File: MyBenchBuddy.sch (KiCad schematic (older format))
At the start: 0 parts

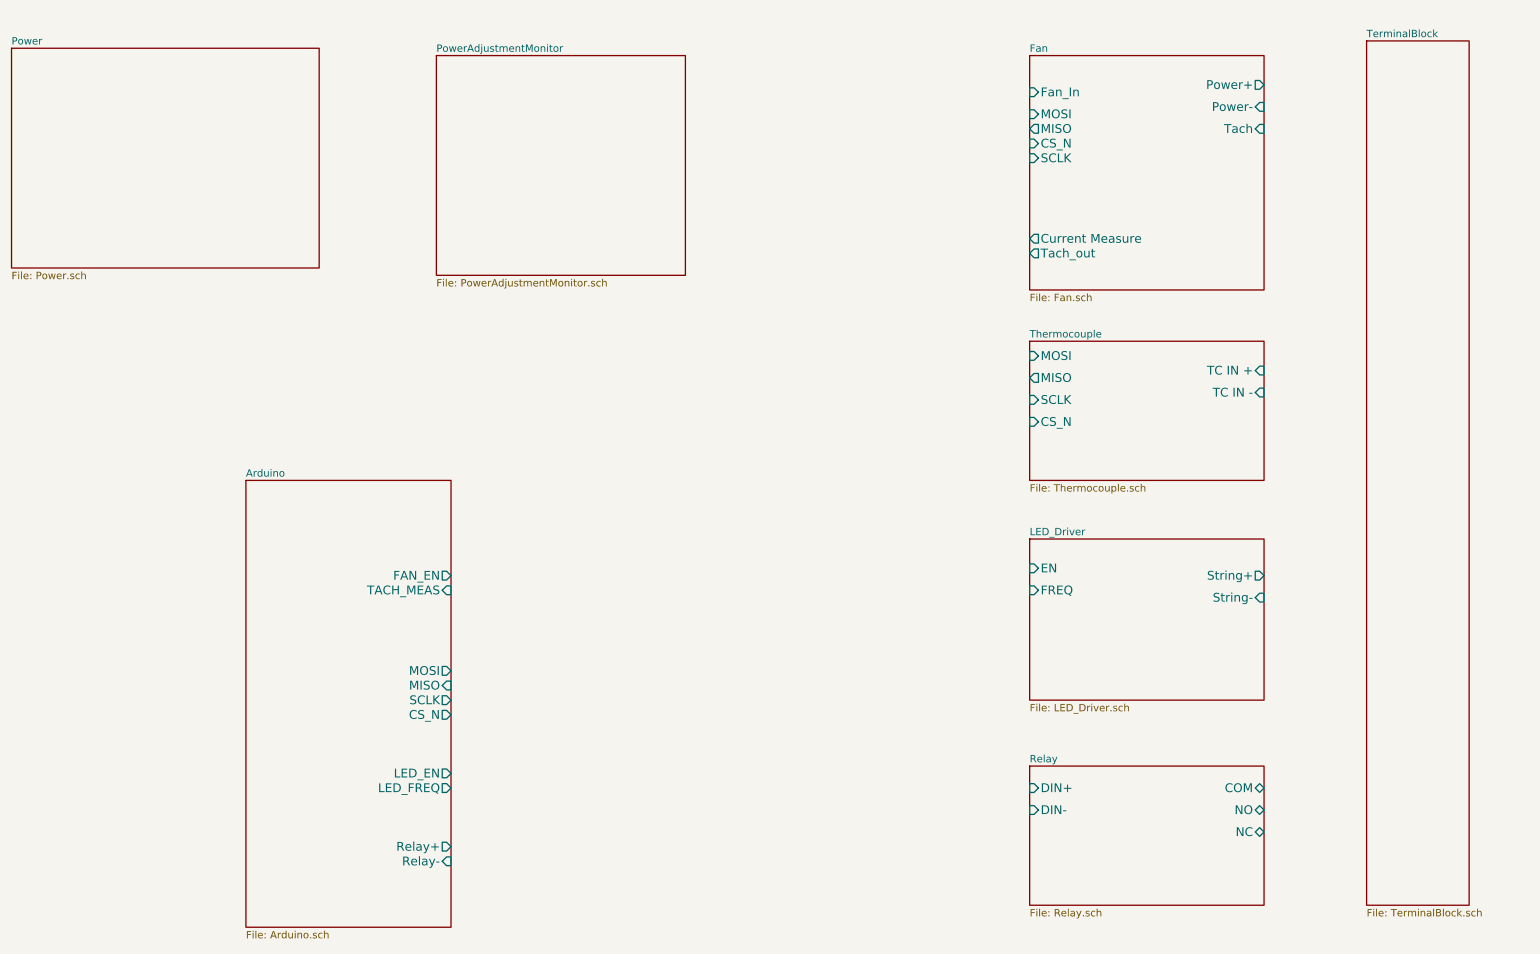
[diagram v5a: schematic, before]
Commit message: Added Power Adjustment And Monitoring
Added generic schematic to the power adjustment and monitoring sheet.
The final version will depend on the parts selected.
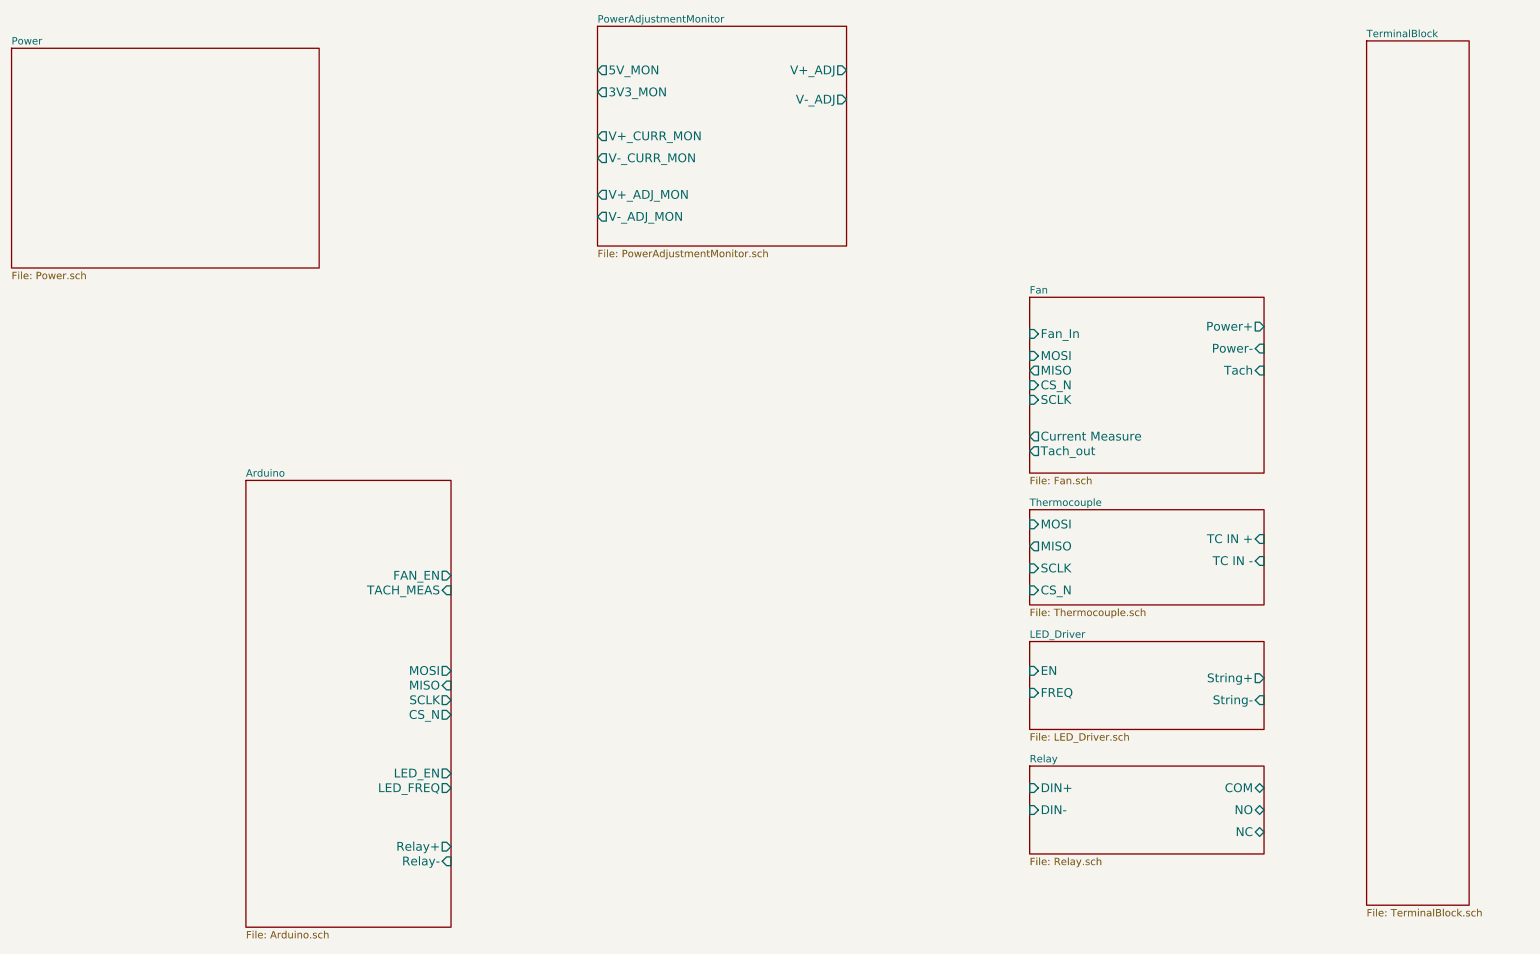
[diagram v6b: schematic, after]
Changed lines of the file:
@@
 $EndSheet
 $Sheet
-S 7900 2950 1600 950
+S 7900 4100 1600 650
 U 52340B73
 F0 "Thermocouple" 50
 F1 "Thermocouple.sch" 50
-F2 "TC IN +" I R 9500 3150 60
-F3 "TC IN -" I R 9500 3300 60
-F4 "MOSI" I L 7900 3050 60
-F5 "MISO" O L 7900 3200 60
-F6 "SCLK" I L 7900 3350 60
-F7 "CS_N" I L 7900 3500 60
+F2 "TC IN +" I R 9500 4300 60
+F3 "TC IN -" I R 9500 4450 60
+F4 "MOSI" I L 7900 4200 60
+F5 "MISO" O L 7900 4350 60
+F6 "SCLK" I L 7900 4500 60
+F7 "CS_N" I L 7900 4650 60
 $EndSheet
 $Sheet
-S 7900 5850 1600 950
+S 7900 5850 1600 600
 U 52340B96
 F0 "Relay" 50
@@
 $EndSheet
 $Sheet
-S 7900 4300 1600 1100
+S 7900 5000 1600 600
 U 52340BE4
 F0 "LED_Driver" 50
 F1 "LED_Driver.sch" 50
-F2 "EN" I L 7900 4500 60
-F3 "FREQ" I L 7900 4650 60
-F4 "String+" O R 9500 4550 60
-F5 "String-" I R 9500 4700 60
+F2 "EN" I L 7900 5200 60
+F3 "FREQ" I L 7900 5350 60
+F4 "String+" O R 9500 5250 60
+F5 "String-" I R 9500 5400 60
 $EndSheet
 $Sheet
-S 7900 1000 1600 1600
+S 7900 2650 1600 1200
 U 52340C05
 F0 "Fan" 50
 F1 "Fan.sch" 50
-F2 "Power+" O R 9500 1200 60
-F3 "Power-" I R 9500 1350 60
-F4 "Tach" I R 9500 1500 60
-F5 "Tach_out" O L 7900 2350 60
-F6 "Fan_In" I L 7900 1250 60
-F7 "Current Measure" O L 7900 2250 60
-F8 "MOSI" I L 7900 1400 60
-F9 "MISO" O L 7900 1500 60
-F10 "CS_N" I L 7900 1600 60
-F11 "SCLK" I L 7900 1700 60
+F2 "Power+" O R 9500 2850 60
+F3 "Power-" I R 9500 3000 60
+F4 "Tach" I R 9500 3150 60
+F5 "Tach_out" O L 7900 3700 60
+F6 "Fan_In" I L 7900 2900 60
+F7 "Current Measure" O L 7900 3600 60
+F8 "MOSI" I L 7900 3050 60
+F9 "MISO" O L 7900 3150 60
+F10 "CS_N" I L 7900 3250 60
+F11 "SCLK" I L 7900 3350 60
 $EndSheet
 $Sheet
@@
 $EndSheet
 $Sheet
-S 3850 1000 1700 1500
+S 4950 800  1700 1500
 U 523F9073
 F0 "PowerAdjustmentMonitor" 50
 F1 "PowerAdjustmentMonitor.sch" 50
+F2 "V+_ADJ" O R 6650 1100 60
+F3 "V-_ADJ" O R 6650 1300 60
+F4 "3V3_MON" O L 4950 1250 60
+F5 "5V_MON" O L 4950 1100 60
+F6 "V+_ADJ_MON" O L 4950 1950 60
+F7 "V-_ADJ_MON" O L 4950 2100 60
+F8 "V-_CURR_MON" O L 4950 1700 60
+F9 "V+_CURR_MON" O L 4950 1550 60
 $EndSheet
 $EndSCHEMATC

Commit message: Added LED Block
Added LED Block Diagram (version 1)
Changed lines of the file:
@@
 Sheet 1 9
 Title ""
-Date "23 sep 2013"
+Date "28 sep 2013"
 Rev ""
 Comp ""
@@
 $EndSheet
 $Sheet
-S 7900 5000 1600 600
-U 52340BE4
-F0 "LED_Driver" 50
-F1 "LED_Driver.sch" 50
-F2 "EN" I L 7900 5200 60
-F3 "FREQ" I L 7900 5350 60
-F4 "String+" O R 9500 5250 60
-F5 "String-" I R 9500 5400 60
-$EndSheet
-$Sheet
 S 7900 2650 1600 1200
 U 52340C05
@@
 F9 "V+_CURR_MON" O L 4950 1550 60
 $EndSheet
+$Sheet
+S 7900 5000 1600 600
+U 52340BE4
+F0 "LED_Driver" 50
+F1 "LED_Driver.sch" 50
+F2 "String+" O R 9500 5250 60
+F3 "String-" I R 9500 5400 60
+F4 "LED_EN_PWM" I L 7900 5250 60
+$EndSheet
 $EndSCHEMATC

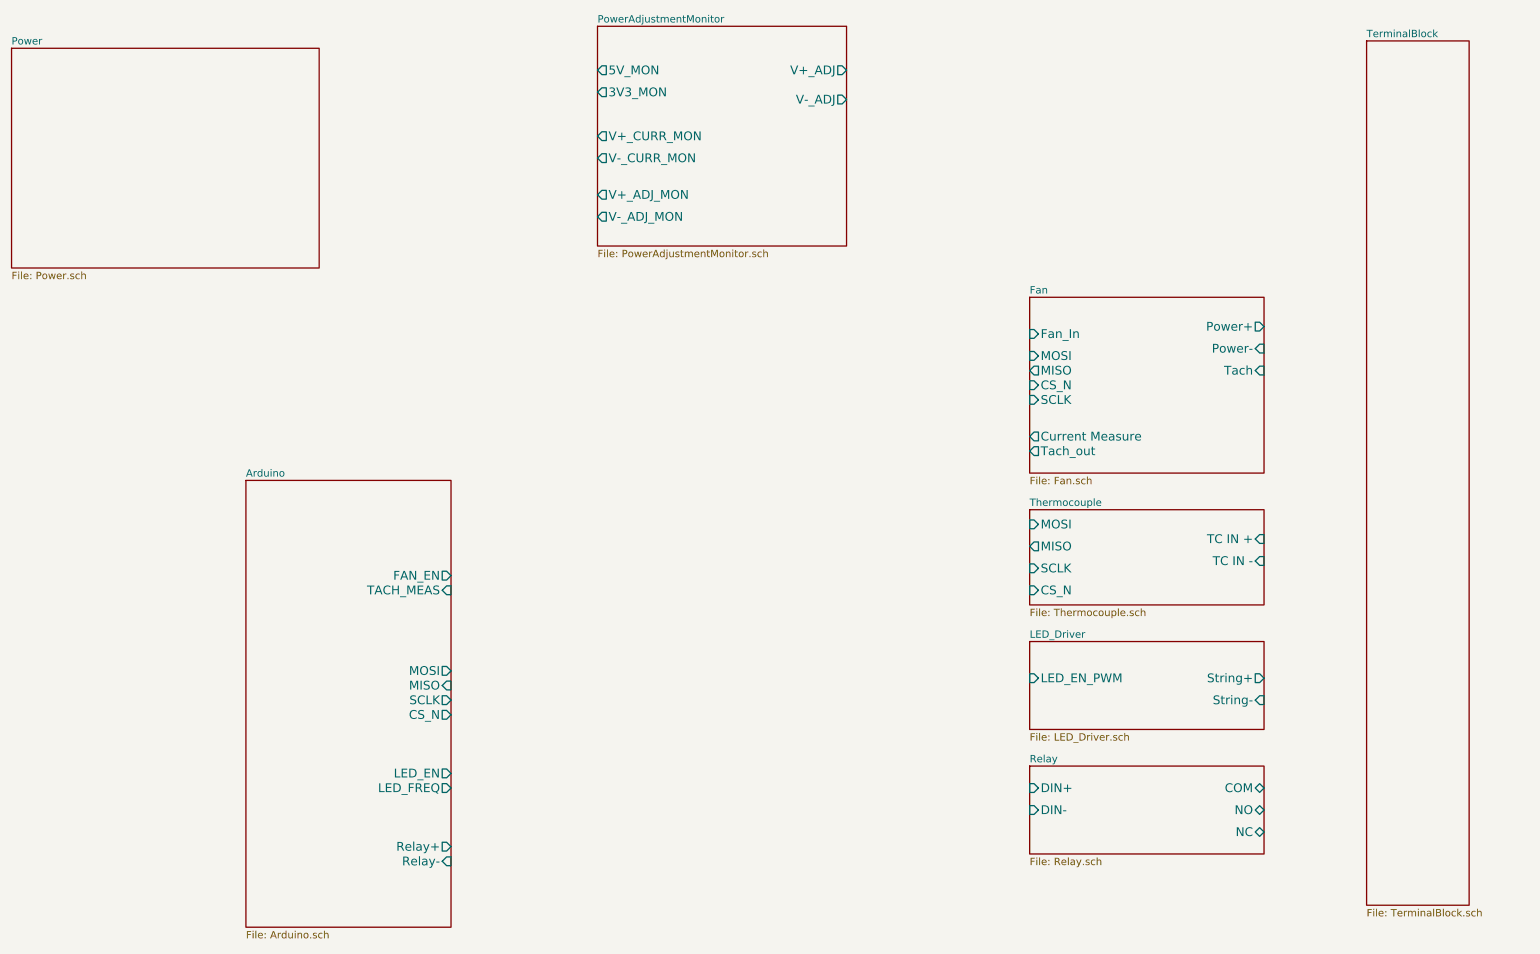
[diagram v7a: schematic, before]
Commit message: Added Arduino Block
Added Arduino Block and connected the top level of the schematic.
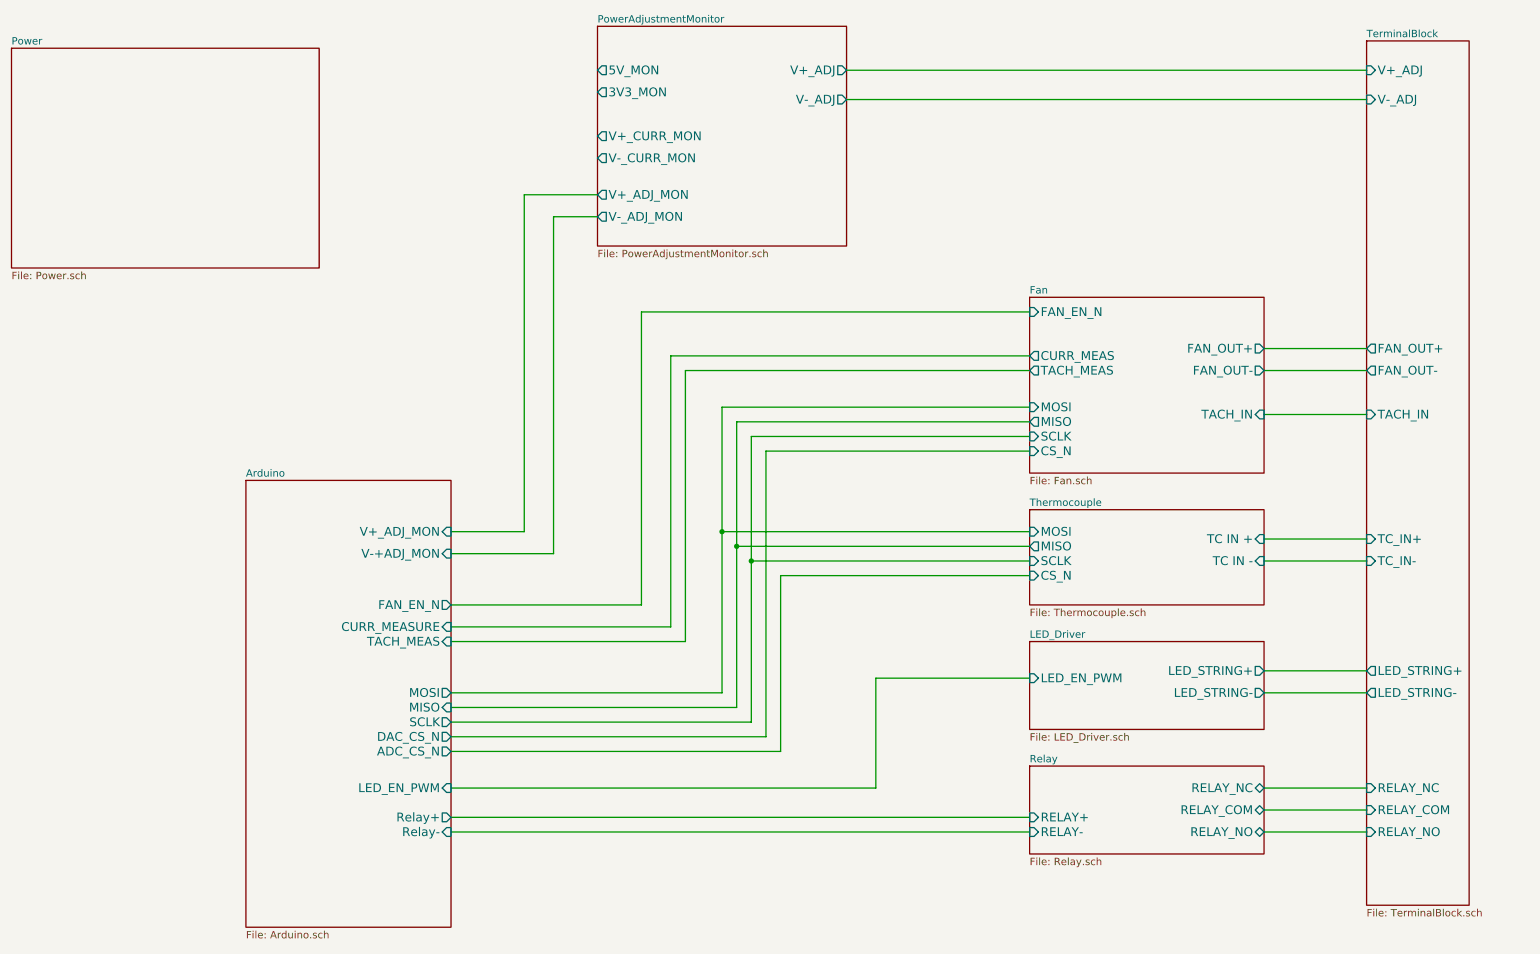
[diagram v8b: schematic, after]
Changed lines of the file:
@@
 $EndDescr
-$Sheet
-S 2550 3900 1400 3050
-U 52340B21
-F0 "Arduino" 50
-F1 "Arduino.sch" 50
-F2 "Relay+" O R 3950 6400 60
-F3 "Relay-" I R 3950 6500 60
-F4 "MOSI" O R 3950 5200 60
-F5 "MISO" I R 3950 5300 60
-F6 "SCLK" O R 3950 5400 60
-F7 "CS_N" O R 3950 5500 60
-F8 "LED_EN" O R 3950 5900 60
-F9 "LED_FREQ" O R 3950 6000 60
-F10 "FAN_EN" O R 3950 4550 60
-F11 "TACH_MEAS" I R 3950 4650 60
-$EndSheet
 $Sheet
 S 7900 4100 1600 650
@@
 F2 "TC IN +" I R 9500 4300 60
 F3 "TC IN -" I R 9500 4450 60
-F4 "MOSI" I L 7900 4200 60
+F4 "MOSI" I L 7900 4250 60
 F5 "MISO" O L 7900 4350 60
-F6 "SCLK" I L 7900 4500 60
-F7 "CS_N" I L 7900 4650 60
+F6 "SCLK" I L 7900 4450 60
+F7 "CS_N" I L 7900 4550 60
 $EndSheet
 $Sheet
@@
 F0 "Relay" 50
 F1 "Relay.sch" 50
-F2 "DIN+" I L 7900 6000 60
-F3 "DIN-" I L 7900 6150 60
-F4 "NC" B R 9500 6300 60
-F5 "NO" B R 9500 6150 60
-F6 "COM" B R 9500 6000 60
+F2 "RELAY_NC" B R 9500 6000 60
+F3 "RELAY_NO" B R 9500 6300 60
+F4 "RELAY_COM" B R 9500 6150 60
+F5 "RELAY+" I L 7900 6200 60
+F6 "RELAY-" I L 7900 6300 60
 $EndSheet
 $Sheet
@@
 F0 "Fan" 50
 F1 "Fan.sch" 50
-F2 "Power+" O R 9500 2850 60
-F3 "Power-" I R 9500 3000 60
-F4 "Tach" I R 9500 3150 60
-F5 "Tach_out" O L 7900 3700 60
-F6 "Fan_In" I L 7900 2900 60
-F7 "Current Measure" O L 7900 3600 60
-F8 "MOSI" I L 7900 3050 60
-F9 "MISO" O L 7900 3150 60
-F10 "CS_N" I L 7900 3250 60
-F11 "SCLK" I L 7900 3350 60
+F2 "MOSI" I L 7900 3400 60
+F3 "MISO" O L 7900 3500 60
+F4 "CS_N" I L 7900 3700 60
+F5 "SCLK" I L 7900 3600 60
+F6 "FAN_OUT+" O R 9500 3000 60
+F7 "TACH_IN" I R 9500 3450 60
+F8 "TACH_MEAS" O L 7900 3150 60
+F9 "FAN_EN_N" I L 7900 2750 60
+F10 "CURR_MEAS" O L 7900 3050 60
+F11 "FAN_OUT-" O R 9500 3150 60
 $EndSheet
 $Sheet
@@
 F0 "TerminalBlock" 50
 F1 "TerminalBlock.sch" 50
+F2 "V+_ADJ" I L 10200 1100 60
+F3 "V-_ADJ" I L 10200 1300 60
+F4 "FAN_OUT+" O L 10200 3000 60
+F5 "FAN_OUT-" O L 10200 3150 60
+F6 "TACH_IN" I L 10200 3450 60
+F7 "LED_STRING+" O L 10200 5200 60
+F8 "LED_STRING-" O L 10200 5350 60
+F9 "TC_IN+" I L 10200 4300 60
+F10 "TC_IN-" I L 10200 4450 60
+F11 "RELAY_COM" I L 10200 6150 60
+F12 "RELAY_NO" I L 10200 6300 60
+F13 "RELAY_NC" I L 10200 6000 60
 $EndSheet
 $Sheet
@@
 F0 "LED_Driver" 50
 F1 "LED_Driver.sch" 50
-F2 "String+" O R 9500 5250 60
-F3 "String-" I R 9500 5400 60
-F4 "LED_EN_PWM" I L 7900 5250 60
-$EndSheet
+F2 "LED_EN_PWM" I L 7900 5250 60
+F3 "LED_STRING+" O R 9500 5200 60
+F4 "LED_STRING-" O R 9500 5350 60
+$EndSheet
+Wire Wire Line
+	6650 1100 10200 1100
+Wire Wire Line
+	6650 1300 10200 1300
+Wire Wire Line
+	9500 3000 10200 3000
+Wire Wire Line
+	9500 3150 10200 3150
+Wire Wire Line
+	9500 3450 10200 3450
+Wire Wire Line
+	9500 4300 10200 4300
+Wire Wire Line
+	9500 4450 10200 4450
+Wire Wire Line
+	9500 5200 10200 5200
+Wire Wire Line
+	9500 5350 10200 5350
+Wire Wire Line
+	9500 6000 10200 6000
+Wire Wire Line
+	9500 6150 10200 6150
+Wire Wire Line
+	9500 6300 10200 6300
+Wire Wire Line
+	3950 4250 4450 4250
+Wire Wire Line
+	4450 4250 4450 1950
+Wire Wire Line
+	4450 1950 4950 1950
+Wire Wire Line
+	3950 4400 4650 4400
+Wire Wire Line
+	4650 4400 4650 2100
+Wire Wire Line
+	4650 2100 4950 2100
+Wire Wire Line
+	3950 4750 5250 4750
+Wire Wire Line
+	5250 4750 5250 2750
+Wire Wire Line
+	5250 2750 7900 2750
+$Sheet
+S 2550 3900 1400 3050
+U 52340B21
+F0 "Arduino" 50
+F1 "Arduino.sch" 50
+F2 "Relay+" O R 3950 6200 60
+F3 "Relay-" I R 3950 6300 60
+F4 "MOSI" O R 3950 5350 60
+F5 "MISO" I R 3950 5450 60
+F6 "SCLK" O R 3950 5550 60
+F7 "TACH_MEAS" I R 3950 5000 60
+F8 "FAN_EN_N" O R 3950 4750 60
+F9 "CURR_MEASURE" I R 3950 4900 60
+F10 "V+_ADJ_MON" I R 3950 4250 60
+F11 "V-+ADJ_MON" I R 3950 4400 60
+F12 "LED_EN_PWM" I R 3950 6000 60
+F13 "DAC_CS_N" O R 3950 5650 60
+F14 "ADC_CS_N" O R 3950 5750 60
+$EndSheet
+Wire Wire Line
+	3950 5350 5800 5350
+Wire Wire Line
+	5800 5350 5800 3400
+Wire Wire Line
+	5800 3400 7900 3400
+Wire Wire Line
+	3950 5450 5900 5450
+Wire Wire Line
+	5900 5450 5900 3500
+Wire Wire Line
+	5900 3500 7900 3500
+Wire Wire Line
+	3950 5550 6000 5550
+Wire Wire Line
+	6000 5550 6000 3600
+Wire Wire Line
+	6100 5650 3950 5650
+Wire Wire Line
+	7900 4250 5800 4250
+Connection ~ 5800 4250
+Wire Wire Line
+	7900 4350 5900 4350
+Connection ~ 5900 4350
+Wire Wire Line
+	7900 4450 6000 4450
+Connection ~ 6000 4450
+Wire Wire Line
+	6850 5250 6850 6000
+Wire Wire Line
+	6850 5250 7900 5250
+Wire Wire Line
+	3950 4900 5450 4900
+Wire Wire Line
+	5450 4900 5450 3050
+Wire Wire Line
+	5450 3050 7900 3050
+Wire Wire Line
+	3950 5000 5550 5000
+Wire Wire Line
+	5550 5000 5550 3150
+Wire Wire Line
+	5550 3150 7900 3150
+Wire Wire Line
+	6000 3600 7900 3600
+Wire Wire Line
+	3950 6300 7900 6300
+Wire Wire Line
+	7900 6200 3950 6200
+Wire Wire Line
+	6850 6000 3950 6000
+Wire Wire Line
+	6100 3700 6100 5650
+Wire Wire Line
+	6100 3700 7900 3700
+Wire Wire Line
+	3950 5750 6200 5750
+Wire Wire Line
+	6200 5750 6200 4550
+Wire Wire Line
+	6200 4550 7900 4550
 $EndSCHEMATC
